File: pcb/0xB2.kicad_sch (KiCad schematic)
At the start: 40 parts, among them J1 USB_C_Receptacle_USB2.0, J2 Conn_01x12, J3 Conn_01x05, J4 Conn_01x12, J5 Conn_01x02, SW1 SW_Push, SW2 SW_Push, U1 RP2040, U2 GD25Q80CEIGR, U3 XC6210B332MR-G, Y1 Crystal_GND24

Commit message: import
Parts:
- added J6: Ribbon, Connector_PinHeader_2.54mm:PinHeader_1x06_P2.54mm_Vertical, symbol Connector:Conn_01x06_Female
- added J7: Ribbon, Connector_PinHeader_2.54mm:PinHeader_1x05_P2.54mm_Vertical, symbol Connector:Conn_01x05_Female
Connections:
- net A0 renamed row2_r
- net row2_r: now also J7.5 (Pin_5)
- net A1 renamed col1_r
- net col1_r: now also J7.4 (Pin_4)
- net A2 renamed col2_r
- net col2_r: now also J7.3 (Pin_3)
- net A3 renamed row1_r
- net row1_r: now also J7.2 (Pin_2)
- net D21 renamed col3_r
- net col3_r: now also J7.1 (Pin_1)
- net D4 renamed row4_r
- net row4_r: now also J6.1 (Pin_1)
- net D5 renamed row3_r
- net row3_r: now also J6.2 (Pin_2)
- net D6 renamed col4_r
- net col4_r: now also J6.3 (Pin_3)
- net D7 renamed col5_r
- net col5_r: now also J6.4 (Pin_4)
- net D8 renamed col6_r
- net col6_r: now also J6.5 (Pin_5)
- net D9 renamed row5_r
- net row5_r: now also J6.6 (Pin_6)

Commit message: import libs
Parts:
- added H1, H2: M4, Library:MountingHole_4mm_Pad_thin, symbol Mechanical:MountingHole_Pad
- J6: footprint Connector_PinHeader_2.54mm:PinHeader_1x06_P2.54mm_Vertical -> Library:6_PinHeader
- J7: footprint Connector_PinHeader_2.54mm:PinHeader_1x05_P2.54mm_Vertical -> Library:5_PinHeader
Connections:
- net GND: now also H1.1, H2.1
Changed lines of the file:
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@@
       (effects (font (size 1.27 1.27)) (justify left))
     )
-    (property "Footprint" "Connector_PinHeader_2.54mm:PinHeader_1x06_P2.54mm_Vertical" (id 2) (at 316.23 57.15 0)
+    (property "Footprint" "Library:6_PinHeader" (id 2) (at 316.23 57.15 0)
       (effects (font (size 1.27 1.27)) hide)
     )
@@
     (pin "2")
   )
+  (symbol (lib_id "Mechanical:MountingHole_Pad") (at 349.885 30.48 0) (unit 1)
+    (in_bom yes) (on_board yes)
+    (property "Reference" "H1" (id 0) (at 348.615 25.4 0)
+      (effects (font (size 1.27 1.27)) (justify left))
+    )
+    (property "Value" "M4" (id 1) (at 348.615 42.672 0)
+      (effects (font (size 1.27 1.27)) (justify left))
+    )
+    (property "Footprint" "Library:MountingHole_4mm_Pad_thin" (id 2) (at 349.885 30.48 0)
+      (effects (font (size 1.27 1.27)) hide)
+    )
+    (property "Datasheet" "~" (id 3) (at 349.885 30.48 0)
+      (effects (font (size 1.27 1.27)) hide)
+    )
+    (pin "1")
+  )
   (symbol (lib_id "Device:R") (at 24.765 181.61 180) (unit 1)
     (in_bom yes) (on_board yes)
@@
     (pin "2")
   )
+  (symbol (lib_id "Mechanical:MountingHole_Pad") (at 356.235 30.48 0) (unit 1)
+    (in_bom yes) (on_board yes)
+    (property "Reference" "H2" (id 0) (at 354.965 25.4 0)
+      (effects (font (size 1.27 1.27)) (justify left))
+    )
+    (property "Value" "M4" (id 1) (at 354.965 42.672 0)
+      (effects (font (size 1.27 1.27)) (justify left))
+    )
+    (property "Footprint" "Library:MountingHole_4mm_Pad_thin" (id 2) (at 356.235 30.48 0)
+      (effects (font (size 1.27 1.27)) hide)
+    )
+    (property "Datasheet" "~" (id 3) (at 356.235 30.48 0)
+      (effects (font (size 1.27 1.27)) hide)
+    )
+    (pin "1")
+  )
+  (symbol (lib_id "power:GND") (at 356.235 33.02 0) (unit 1)
+    (in_bom yes) (on_board yes)
+    (property "Reference" "#PWR032" (id 0) (at 356.235 39.37 0)
+      (effects (font (size 1.27 1.27)) hide)
+    )
+    (property "Value" "GND" (id 1) (at 356.079 40.0049 90)
+      (effects (font (size 1.27 1.27)) (justify left))
+    )
+    (property "Footprint" "" (id 2) (at 356.235 33.02 0)
+      (effects (font (size 1.27 1.27)) hide)
+    )
+    (property "Datasheet" "" (id 3) (at 356.235 33.02 0)
+      (effects (font (size 1.27 1.27)) hide)
+    )
+    (pin "1")
+  )
   (symbol (lib_id "power:+3.3V") (at 58.42 109.22 0) (unit 1)
     (in_bom yes) (on_board yes)
@@
       (effects (font (size 1.27 1.27)) (justify left))
     )
-    (property "Footprint" "Connector_PinHeader_2.54mm:PinHeader_1x05_P2.54mm_Vertical" (id 2) (at 339.09 58.42 0)
+    (property "Footprint" "Library:5_PinHeader" (id 2) (at 339.09 58.42 0)
       (effects (font (size 1.27 1.27)) hide)
     )
@@
     (pin "1")
   )
+  (symbol (lib_id "power:GND") (at 349.885 33.02 0) (unit 1)
+    (in_bom yes) (on_board yes)
+    (property "Reference" "#PWR031" (id 0) (at 349.885 39.37 0)
+      (effects (font (size 1.27 1.27)) hide)
+    )
+    (property "Value" "GND" (id 1) (at 349.729 40.0049 90)
+      (effects (font (size 1.27 1.27)) (justify left))
+    )
+    (property "Footprint" "" (id 2) (at 349.885 33.02 0)
+      (effects (font (size 1.27 1.27)) hide)
+    )
+    (property "Datasheet" "" (id 3) (at 349.885 33.02 0)
+      (effects (font (size 1.27 1.27)) hide)
+    )
+    (pin "1")
+  )
   (symbol (lib_id "Device:C") (at 130.81 180.34 0) (unit 1)
     (in_bom yes) (on_board yes)
@@
       (reference "#PWR030") (unit 1) (value "GND") (footprint "")
     )
+    (path "/e3b3a6b6-6db7-40b6-bd0d-59e70b5a4bd4"
+      (reference "#PWR031") (unit 1) (value "GND") (footprint "")
+    )
+    (path "/90f4e940-8051-4b36-9286-f494572b14b9"
+      (reference "#PWR032") (unit 1) (value "GND") (footprint "")
+    )
     (path "/da1644f7-6b59-4f28-b4bd-963f2f055bce"
       (reference "#PWR0101") (unit 1) (value "GND") (footprint "")
@@
       (reference "FB1") (unit 1) (value "FerriteBead_Small") (footprint "Inductor_SMD:L_0603_1608Metric")
     )
+    (path "/7e27e11b-0033-4f6c-a305-222116b5af33"
+      (reference "H1") (unit 1) (value "M4") (footprint "Library:MountingHole_4mm_Pad_thin")
+    )
+    (path "/909539b0-d574-4da4-8d79-48e0f3a24595"
+      (reference "H2") (unit 1) (value "M4") (footprint "Library:MountingHole_4mm_Pad_thin")
+    )
     (path "/6125bb34-31fe-49ed-b2ab-61dab24d450a"
       (reference "J1") (unit 1) (value "USB_C_Receptacle_USB2.0") (footprint "0xLib_USB_Type-C:USB_C_Receptacle_HRO_TYPE-C-31-M-14")
@@
     )
     (path "/08eed42f-b0b5-4dbc-8033-da3ce74644a6"
-      (reference "J6") (unit 1) (value "Ribbon") (footprint "Connector_PinHeader_2.54mm:PinHeader_1x06_P2.54mm_Vertical")
+      (reference "J6") (unit 1) (value "Ribbon") (footprint "Library:6_PinHeader")
     )
     (path "/b4f3deb9-ff7a-4ab8-aa63-bde787a78d58"
-      (reference "J7") (unit 1) (value "Ribbon") (footprint "Connector_PinHeader_2.54mm:PinHeader_1x05_P2.54mm_Vertical")
+      (reference "J7") (unit 1) (value "Ribbon") (footprint "Library:5_PinHeader")
     )
     (path "/81213cff-519c-4fcf-ae25-6fad0fc859bb"

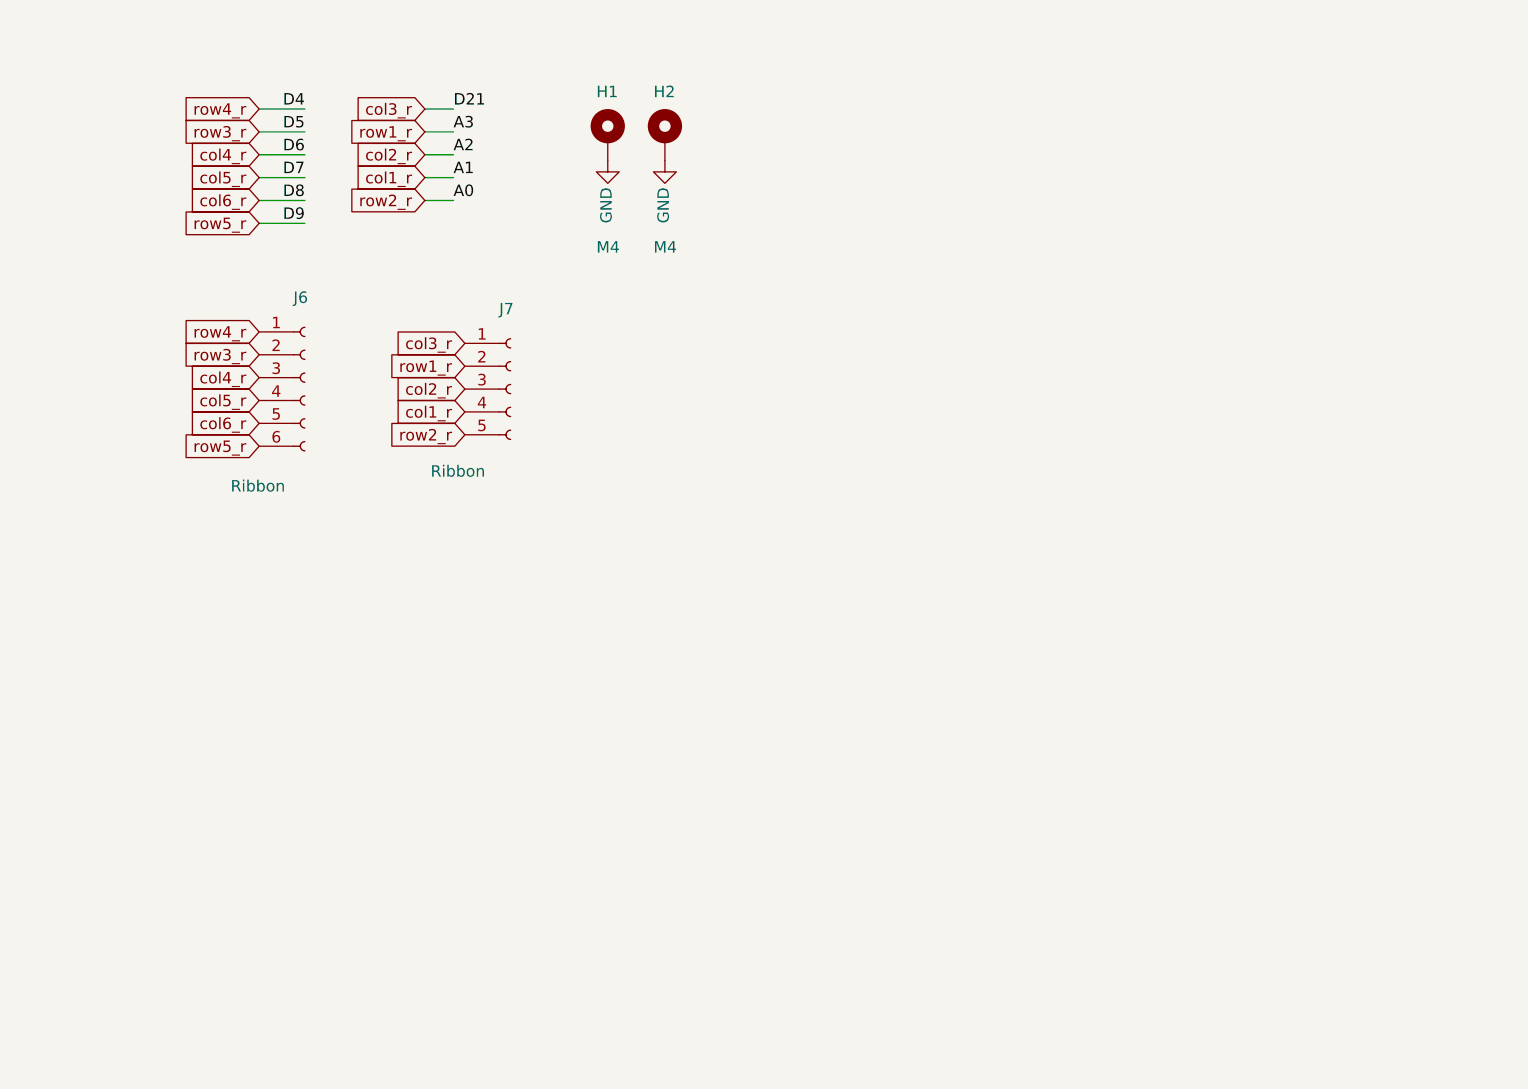
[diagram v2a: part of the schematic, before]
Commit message: add new and remove old connectors
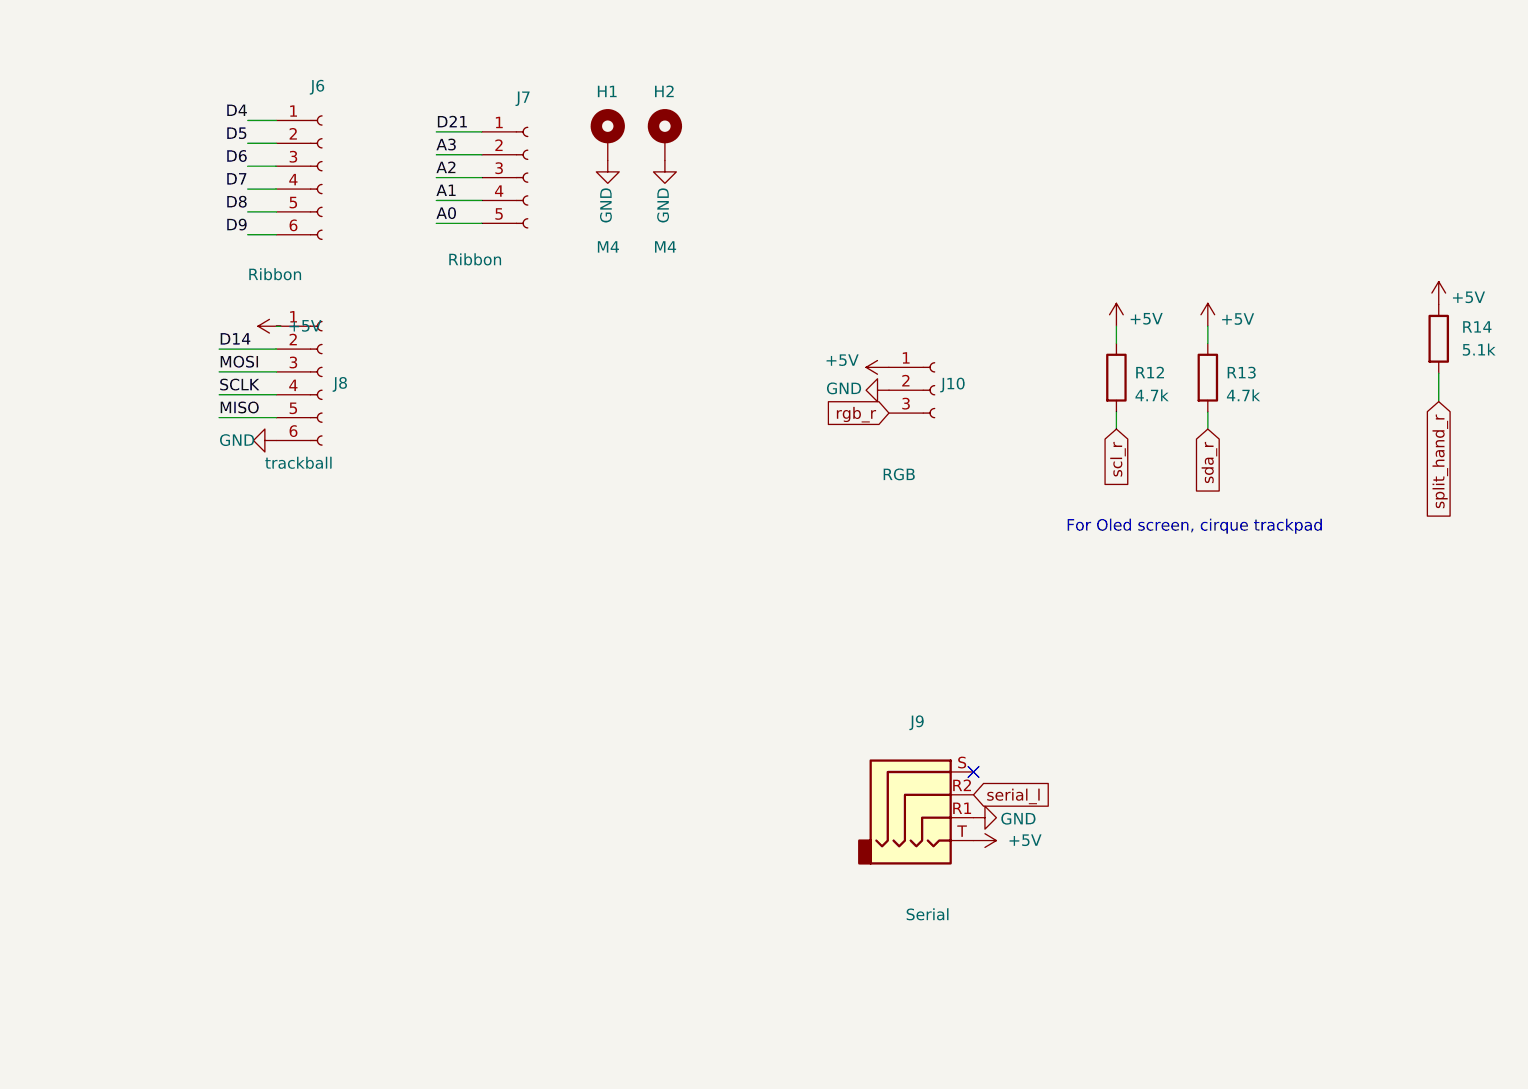
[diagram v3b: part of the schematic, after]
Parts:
- added J10: RGB, Library:header1x03, symbol Connector:Conn_01x03_Female
- added J8: trackball, Library:6_PinHeader, symbol Connector:Conn_01x06_Female
- added J9: Serial, Library:Jack_3.5mm_PJ320E_Horizontal, symbol Connector:AudioJack4
- added R12, R13: 4.7k, Library:R_1206_handsolder, symbol Device:R
- added R14: 5.1k, Library:R_1206_handsolder, symbol Device:R
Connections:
- net +5V: now also J10.1 (Pin_1), J8.1 (Pin_1), J9.T, R12.1, R13.1, R14.1
- net D14: now also J8.2 (Pin_2)
- net GND: now also J10.2 (Pin_2), J8.6 (Pin_6), J9.R1
- net MISO: now also J8.5 (Pin_5)
- net MOSI: now also J8.3 (Pin_3)
- net SCLK: now also J8.4 (Pin_4)
- net col1_r renamed A1
- net col2_r renamed A2
- net col3_r renamed D21
- net col4_r renamed D6
- net col5_r renamed D7
- net col6_r renamed D8
- net row1_r renamed A3
- net row2_r renamed A0
- net row3_r renamed D5
- net row4_r renamed D4
- net row5_r renamed D9
- new net rgb_r: J10.3 (Pin_3)
- new net scl_r: R12.2
- new net sda_r: R13.2
- new net serial_l: J9.R2
- new net split_hand_r: R14.2
- no-connect marks 9 -> 10
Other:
- note added: "For Oled screen, cirque trackpad"
- moved on the sheet: J6, J7

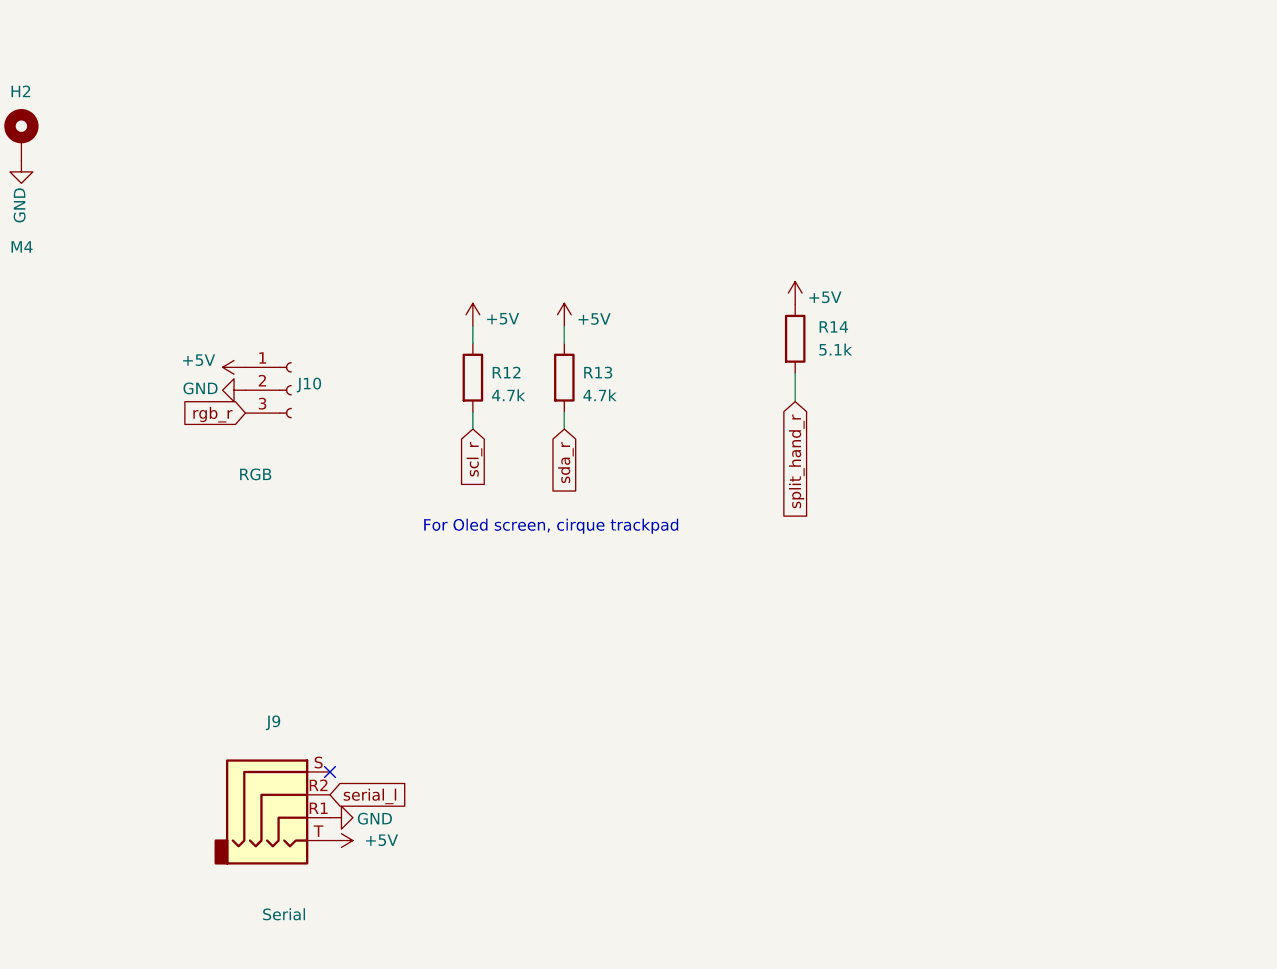
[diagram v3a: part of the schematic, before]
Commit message: add reversible reset button
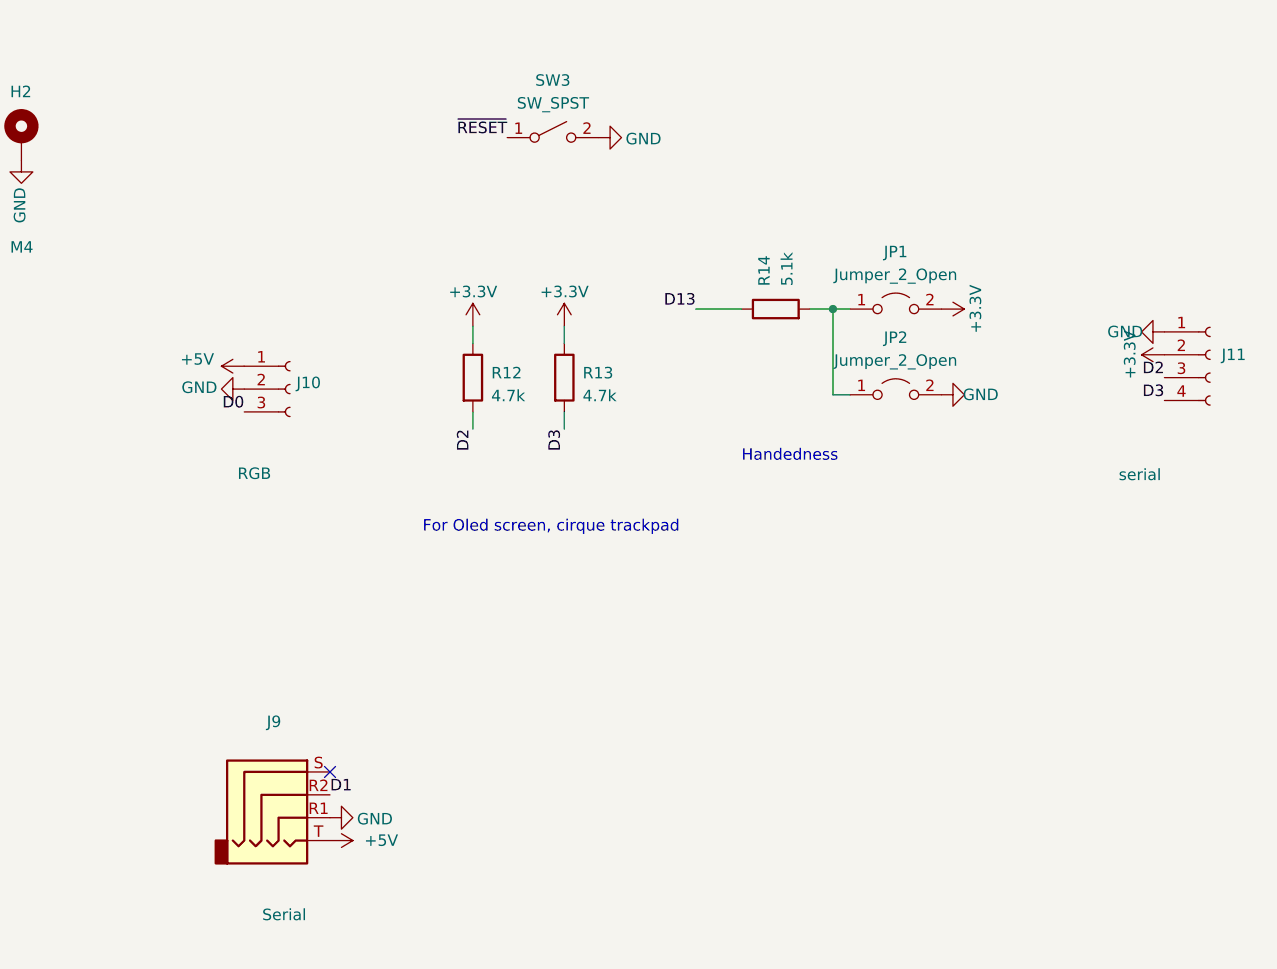
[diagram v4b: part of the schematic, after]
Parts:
- added J11: serial, Library:PinHeader_1x04_P2.54mm_Vertical, symbol Connector:Conn_01x04_Female
- added JP1, JP2: Jumper_2_Open, symbol Jumper:Jumper_2_Open
- added SW3: SW_SPST, Library:PushSwitch, symbol Switch:SW_SPST
- R12, R13, R14: footprint Library:R_1206_handsolder -> Resistor_SMD:R_0402_1005Metric
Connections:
- net rgb_r is gone; now on net D0: J10.3 (Pin_3)
- net scl_r is gone; now on net D2: R12.2
- net sda_r is gone; now on net D3: R13.2
- net serial_l is gone; now on net D1: J9.R2
- net +3V3: now also R12.1, R13.1, J11.2 (Pin_2), JP1.2 (B)
- net +5V: no longer R12.1, R13.1, R14.1
- net D13: now also R14.1
- net D2: now also J11.3 (Pin_3)
- net D3: now also J11.4 (Pin_4)
- net GND: now also J11.1 (Pin_1), JP2.2 (B), SW3.2 (B)
- net ~{RESET}: now also SW3.1 (A)
- net split_hand_r: no longer names the net of R14.2
- net split_hand_r: now also JP1.1 (A), JP2.1 (A)
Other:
- note added: "Handedness"
